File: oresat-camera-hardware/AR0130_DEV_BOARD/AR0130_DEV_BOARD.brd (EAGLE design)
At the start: 40 x 44 mm, 61 parts, among them J2 4-1734592-0, U10 SN74AVCB164245VR, U11 KC2520B27.0000C10E00, U12 TPS71818-33DRVT, U13 SN74AVCH8T245RHLR, U14 TPS71928-28DRVT, U15 TPS71928-28DRVT, U6 MCP9808T-E/MCDFN8_2X3MC-M, U7 MCP9808T-E/MCDFN8_2X3MC-M, U9 TCA9509DGKRDGK8-M

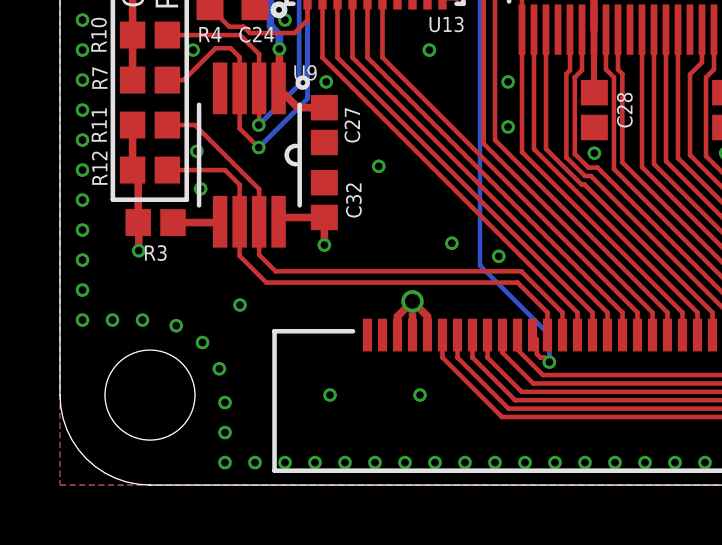
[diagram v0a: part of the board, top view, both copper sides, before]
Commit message: added a LED
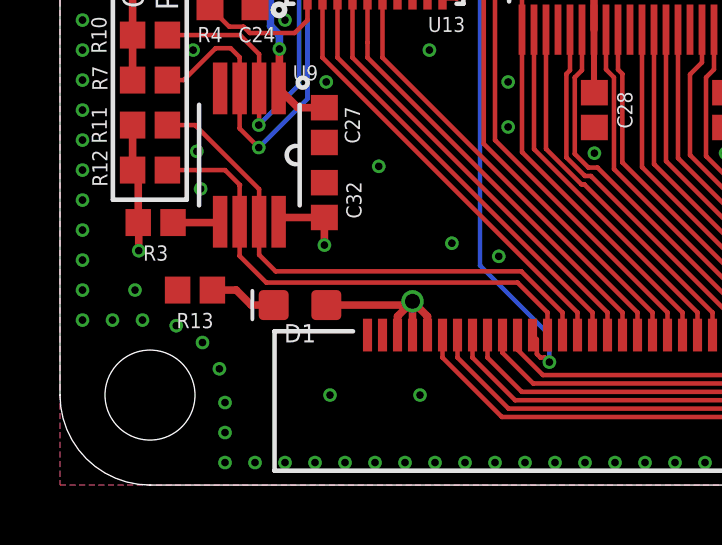
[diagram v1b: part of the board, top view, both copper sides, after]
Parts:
- added D1: (no value), SparkFun-LED:LED-0603
- added R13: (no value), SparkFun-Resistors:0402
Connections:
- new net N$2: D1.C, R13.1
- net 5V: now also D1.A
- net GND: now also R13.2
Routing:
- net 5V: track 45.9 -> 48.8 mm
- net N$2: track 0.00 -> 2.25 mm
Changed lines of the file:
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@@
 <drawing>
 <settings>
-<setting alwaysvectorfont="yes"/>
+<setting alwaysvectorfont="no"/>
 <setting verticaltext="up"/>
 </settings>
-<grid distance="0.5" unitdist="mm" unit="mm" style="lines" multiple="1" display="yes" altdistance="0.0625" altunitdist="mm" altunit="mm"/>
+<grid distance="0.5" unitdist="mm" unit="mm" style="lines" multiple="1" display="yes" altdistance="0.0125" altunitdist="mm" altunit="mm"/>
 <layers>
 <layer number="1" name="Top" color="4" fill="1" visible="yes" active="yes"/>
@@
 <attribute name="VALUE" x="32.4335" y="28.619" size="0.0254" layer="27"/>
 </element>
+<element name="D1" library="SparkFun-LED" package="LED-0603" value="" x="8" y="6" rot="R180"/>
+<element name="R13" library="SparkFun-Resistors" library_urn="urn:adsk.eagle:library:2058534" package="0402" package3d_urn="urn:adsk.eagle:package:2058625/2" value=" " x="4.5" y="6.5" rot="R180">
+<attribute name="PROD_ID" value=" " x="7.5" y="3" size="1.778" layer="27" rot="R180" display="off"/>
+</element>
 </elements>
 <signals>
@@
 <wire x1="31" y1="20.1875" x2="31" y2="20.5" width="0.254" layer="16"/>
 <wire x1="31.1875" y1="24.5" x2="31" y2="24.6875" width="0.254" layer="16"/>
+<contactref element="D1" pad="A"/>
+<wire x1="8.877" y1="6" x2="11.625" y2="6" width="0.254" layer="1"/>
+<wire x1="11.625" y1="6" x2="11.75" y2="6.125" width="0.254" layer="1"/>
 </signal>
 <signal name="GND">
@@
 <via x="27" y="12" extent="1-16" drill="0.254"/>
 <via x="29.5" y="10.5" extent="1-16" drill="0.254"/>
-<via x="6" y="6" extent="1-16" drill="0.254"/>
+<via x="2.5" y="6.5" extent="1-16" drill="0.254"/>
 <via x="9" y="3" extent="1-16" drill="0.254"/>
 <via x="12" y="3" extent="1-16" drill="0.254"/>
@@
 <via x="10.3125" y="30.5625" extent="1-16" drill="0.254"/>
 <via x="9" y="31.875" extent="1-16" drill="0.254"/>
+<contactref element="R13" pad="2"/>
 </signal>
 <signal name="3.3V">
@@
 <wire x1="9.5" y1="25.3128" x2="9.5" y2="25" width="0.254" layer="1"/>
 </signal>
+<signal name="N$2">
+<contactref element="R13" pad="1"/>
+<contactref element="D1" pad="C"/>
+<wire x1="7.123" y1="6" x2="6.375" y2="6" width="0.254" layer="1"/>
+<wire x1="5.875" y1="6.5" x2="5.08" y2="6.5" width="0.254" layer="1"/>
+<wire x1="6.375" y1="6" x2="5.875" y2="6.5" width="0.254" layer="1"/>
+</signal>
 </signals>

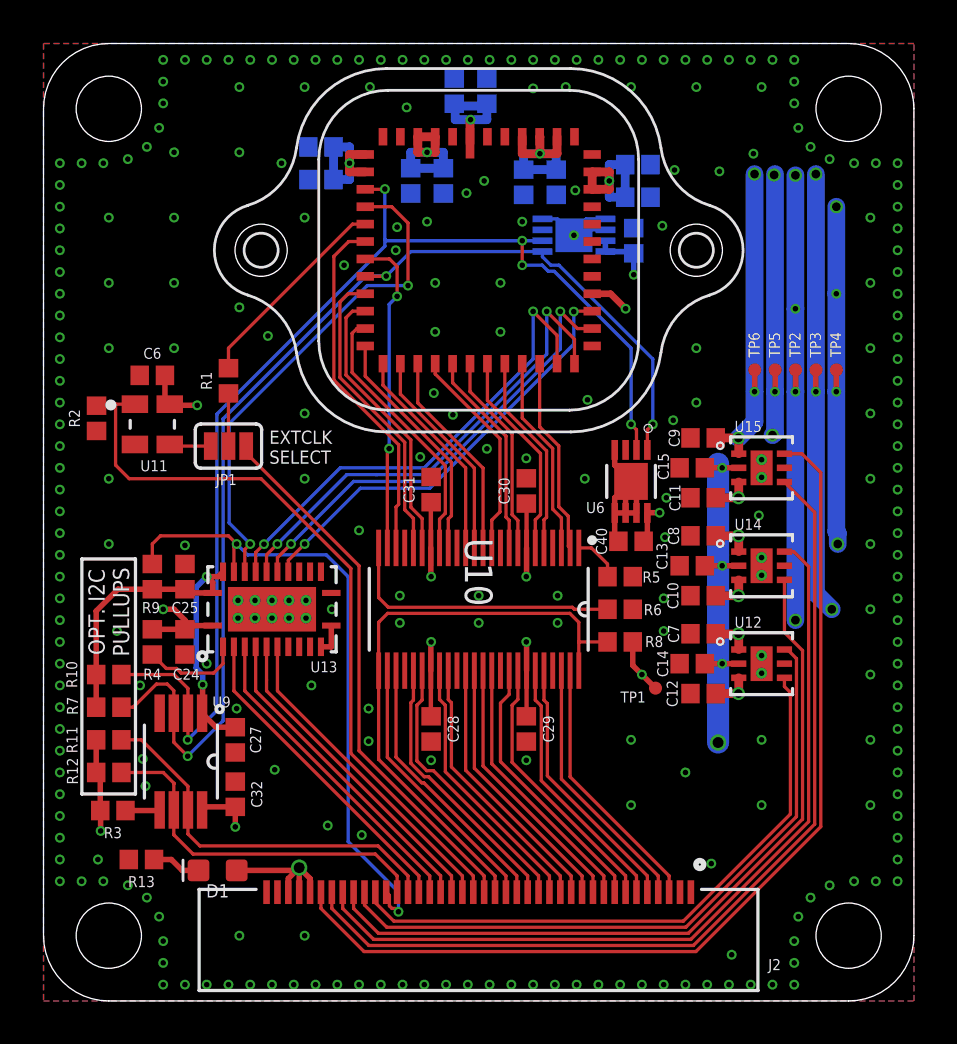
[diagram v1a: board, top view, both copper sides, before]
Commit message: cleaned up some routing, added some test points
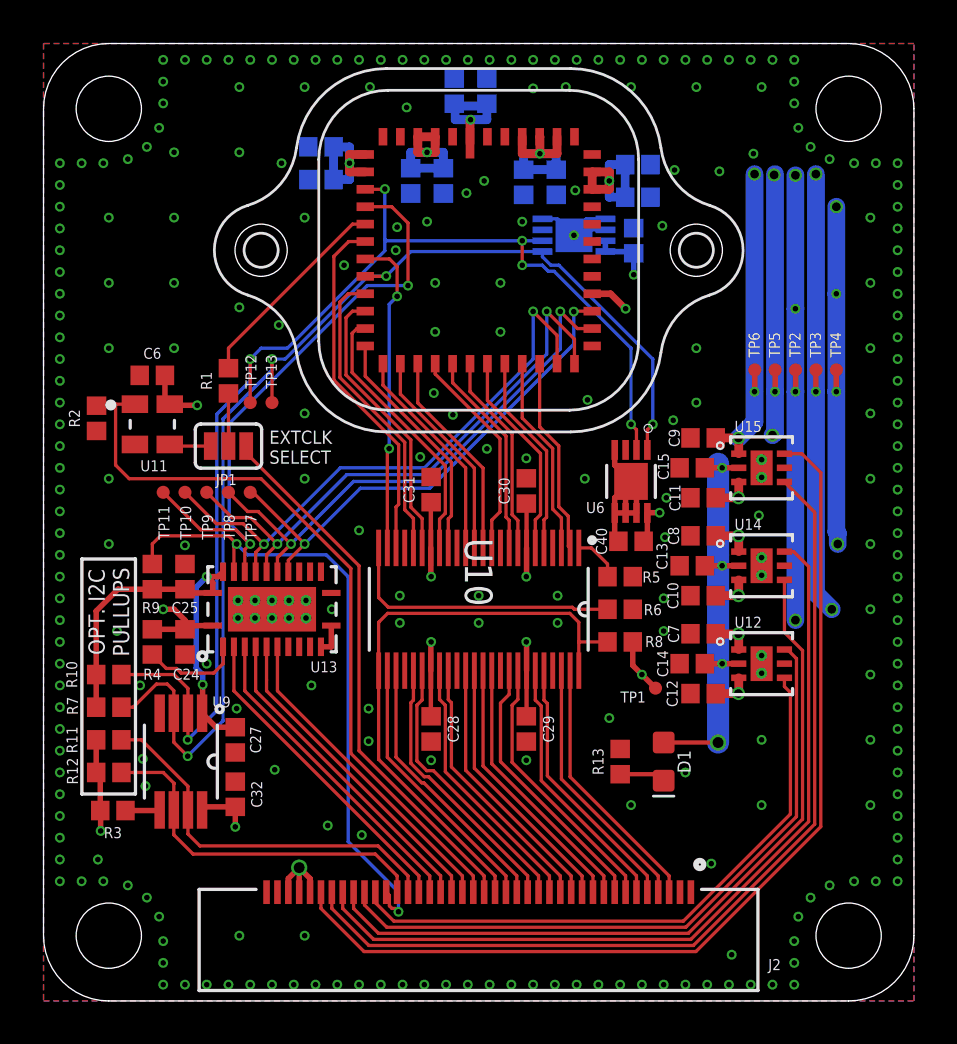
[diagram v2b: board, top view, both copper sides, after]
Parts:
- added TP10, TP11, TP12, TP13, TP7, TP8, TP9: TPTP06R, testpad:TP06R
- moved R13 22.5 mm to (26.5, 11.0), turned to 90 degrees
- moved D1 21.1 mm to (28.5, 11.0), turned to 270 degrees
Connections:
- net OE_BAR_I: now also TP8.TP
- net RST_BAR_I: now also TP9.TP
- net SADDR_I: now also TP11.TP
- net SCL_I: now also TP12.TP
- net SDA_I: now also TP13.TP
- net STANDBY_I: now also TP10.TP
- net TRIG_I: now also TP7.TP
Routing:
- net SADDR_I: track 23.3 -> 28.3 mm
- net STANDBY_I: track 22.4 -> 27.0 mm
- net RST_BAR_I: track 22.4 -> 26.6 mm
- net OE_BAR_I: track 21.1 -> 25.0 mm
- net TRIG_I: track 20.1 -> 23.6 mm
- net SCL_I: track 55.4 -> 58.1 mm, vias 5 -> 6
- net SDA_I: track 52.8 -> 55.1 mm, vias 3 -> 4

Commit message: i dont know what changed, deal with it
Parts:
- C1, C2, C3, C4, C5: device Oliver_Custom:0402 -> SparkFun-Capacitors:0603
- R1: value (none) -> 100
- R10, R11, R12, R2, R3, R4, R5, R6, R7, R8, R9: value (none) -> 10k
- R13: value (none) -> 1k
- moved C22 2.92 mm to (21.0, 39.8), turned to 180 degrees
- moved C3 2.29 mm to (24.6, 39.7), turned to 180 degrees
- moved C21 2.22 mm to (24.2, 38.2), turned to 180 degrees
- moved C4 1.15 mm to (21.4, 41.2), turned to 180 degrees
- moved C1 0.38 mm to (18.4, 37.3)
- moved C2 0.38 mm to (12.4, 37.8)
- moved C5 0.38 mm to (27.7, 38.4)
- moved C23 0.06 mm to (27.3, 37.0)
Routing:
- net VCC_1: track 50.1 -> 50.7 mm

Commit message: final board revisions
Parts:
- U$2: value AR0130CSSM00SPCA0−DRBR1-847AC -> AR0130CSSM00SPCA0−DRBR1-847AB; device Oliver_Custom:AR0130CSSM00SPCA0−DRBR1-847AC -> Oliver_Custom:AR0130CSSM00SPCA0−DRBR1-847AB
- moved C4 3.88 mm to (17.5, 41.1), turned to 0 degrees
- moved C3 3.67 mm to (21.2, 41.1), turned to 0 degrees
- moved C21 3.13 mm to (21.4, 39.6), turned to 0 degrees
- moved C22 3.07 mm to (17.9, 39.6), turned to 0 degrees
- moved TP12 2.72 mm to (9.50, 30.2)
- moved TP13 2.72 mm to (10.5, 30.2)
- moved C19 1.04 mm to (17.4, 36.8)
- moved C1 1.01 mm to (18.8, 36.4)
- moved C20 0.78 mm to (13.2, 38.7)
- moved C2 0.75 mm to (12.9, 37.2)
- moved U7 0.50 mm to (23.9, 35.2)
- moved C23 0.32 mm to (27.0, 36.9)
- moved C5 0.32 mm to (27.4, 38.4)
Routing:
- net VCC: track 34.3 -> 44.9 mm, vias 4 -> 6
- net 2.8V: track 133.0 -> 125.5 mm, vias 13 -> 14
- net VCC_2: track 35.1 -> 39.4 mm, vias 5 -> 7
- net 1.8V: track 61.5 -> 58.2 mm, vias 7 -> 8
- net VCC_1: track 50.7 -> 52.9 mm, vias 5 -> 7
- net SADDR_I: track 28.3 -> 26.2 mm
- net FLASH_I: track 14.7 -> 16.3 mm
- net SDA_I: track 55.1 -> 53.8 mm
- net SCL_I: track 58.1 -> 57.1 mm
- net GND: track 15.4 -> 16.4 mm, vias 256 -> 254
- net DI_0: track 9.05 -> 9.91 mm
- net DI_1: track 9.21 -> 10.0 mm
- net DI_2: track 9.31 -> 10.1 mm
- net DI_3: track 9.58 -> 10.3 mm
- net DI_4: track 9.38 -> 10.1 mm
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
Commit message: more final touches on bouard
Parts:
- moved R13 0.50 mm to (27.0, 11.0)
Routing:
- net 5V: track 48.4 -> 65.4 mm, vias 5 -> 21
- net GND: track 16.4 -> 24.4 mm, vias 254 -> 255
- net VDD18_EN: track 31.0 -> 31.5 mm
- net N$2: track 2.12 -> 1.62 mm

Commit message: yada yada yada
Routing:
- net 5V: track 65.4 -> 70.4 mm
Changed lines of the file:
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@@
 <element name="U9" library="Oliver_Custom" package="DGK8-M" value="TCA9509DGKRDGK8-M" x="6.3125" y="11" smashed="yes" rot="R270">
 <attribute name="MANUFACTURER_PART_NUMBER" value="TCA9509DGKR" x="6.3125" y="11" size="1.778" layer="27" rot="R270" display="off"/>
-<attribute name="NAME" x="7.7574" y="13.4915" size="0.5" layer="25" font="vector" ratio="15" rot="SR0"/>
+<attribute name="NAME" x="8.2574" y="11.9915" size="0.5" layer="25" font="vector" ratio="15" rot="SR0"/>
 <attribute name="VENDOR" value="Texas Instruments" x="6.3125" y="11" size="1.778" layer="27" rot="R270" display="off"/>
 </element>
 <element name="U10" library="Oliver_Custom" package="DGV48" value="SN74AVCB164245VR" x="20" y="18" smashed="yes" rot="R270">
 <attribute name="MANUFACTURER_PART_NUMBER" value="SN74AVCB164245VR" x="20" y="18" size="1.778" layer="27" rot="R270" display="off"/>
-<attribute name="NAME" x="19.365" y="21.2766" size="1.27" layer="25" ratio="6" rot="SR270"/>
+<attribute name="NAME" x="15.2234" y="13.6775" size="0.5" layer="25" font="vector" ratio="15" rot="SR0"/>
 <attribute name="VENDOR" value="Texas Instruments" x="20" y="18" size="1.778" layer="27" rot="R270" display="off"/>
 </element>
@@
 <wire x1="30.5" y1="12" x2="31.5" y2="12" width="1.27" layer="16"/>
 <wire x1="30.5" y1="12" x2="30.5" y2="12.5" width="1.27" layer="16"/>
-<wire x1="30.5" y1="12.5" x2="30.5" y2="11.5" width="1.27" layer="16"/>
 <wire x1="31.5" y1="11.5" x2="31.5" y2="12.5" width="1.27" layer="16"/>
 <wire x1="30.5" y1="11.5" x2="31.5" y2="11.5" width="1.27" layer="16"/>
@@
 <wire x1="31.1875" y1="15.75" x2="31.1875" y2="15.5" width="0.508" layer="1"/>
 <wire x1="31.1875" y1="15.5" x2="31.1875" y2="15.25" width="0.508" layer="1"/>
-<wire x1="30.3925" y1="15.5" x2="31.1875" y2="15.5" width="0.6096" layer="1"/>
+<wire x1="30.3925" y1="15.5" x2="31.1875" y2="15.5" width="0.8128" layer="1"/>
 <wire x1="31.1875" y1="15.5" x2="31.95" y2="15.5" width="0.4064" layer="1"/>
 <via x="31.1875" y="19.75" extent="1-16" drill="0.254"/>
 <wire x1="31.1875" y1="19.75" x2="31.1875" y2="20.25" width="0.6096" layer="1"/>
-<wire x1="30.3925" y1="20" x2="30.9375" y2="20" width="0.6096" layer="1"/>
+<wire x1="30.3925" y1="20" x2="30.9375" y2="20" width="0.8128" layer="1"/>
 <wire x1="30.9375" y1="20" x2="31.1875" y2="19.75" width="0.6096" layer="1" curve="-90"/>
 <wire x1="31.95" y1="20" x2="31.4375" y2="20" width="0.4064" layer="1"/>
@@
 <via x="31.1875" y="24.25" extent="1-16" drill="0.254"/>
 <wire x1="31.1875" y1="24.75" x2="31.1875" y2="24.25" width="0.6096" layer="1"/>
-<wire x1="30.3925" y1="24.5" x2="30.9375" y2="24.5" width="0.6096" layer="1"/>
+<wire x1="30.3925" y1="24.5" x2="30.9375" y2="24.5" width="0.8128" layer="1"/>
 <wire x1="30.9375" y1="24.5" x2="31.1875" y2="24.75" width="0.6096" layer="1" curve="90"/>
 <wire x1="31.95" y1="24.5" x2="31.4375" y2="24.5" width="0.4064" layer="1"/>
@@
 <wire x1="31.5" y1="12.5" x2="31" y2="12.5" width="0.6096" layer="16"/>
 <wire x1="31" y1="12.5" x2="30.8125" y2="12.5" width="0.6096" layer="16"/>
+<wire x1="31" y1="12.5" x2="31" y2="11.5" width="0.6096" layer="1"/>
+<wire x1="30.5" y1="12.5" x2="30.5" y2="11.5" width="0.6096" layer="1"/>
+<wire x1="31" y1="12.5" x2="31" y2="11.5" width="0.6096" layer="1"/>
+<wire x1="31.5" y1="12.5" x2="31.5" y2="11.5" width="0.6096" layer="1"/>
+<wire x1="30.5" y1="12.5" x2="31.5" y2="12.5" width="0.6096" layer="1"/>
+<wire x1="30.5" y1="11.5" x2="31.5" y2="11.5" width="0.6096" layer="1"/>
 </signal>
 <signal name="GND">
